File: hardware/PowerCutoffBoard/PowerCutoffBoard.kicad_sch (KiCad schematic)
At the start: 5 parts, among them U1 STM32G431CBUx, U2 MIC4427, U3 MCP2562-E-SN

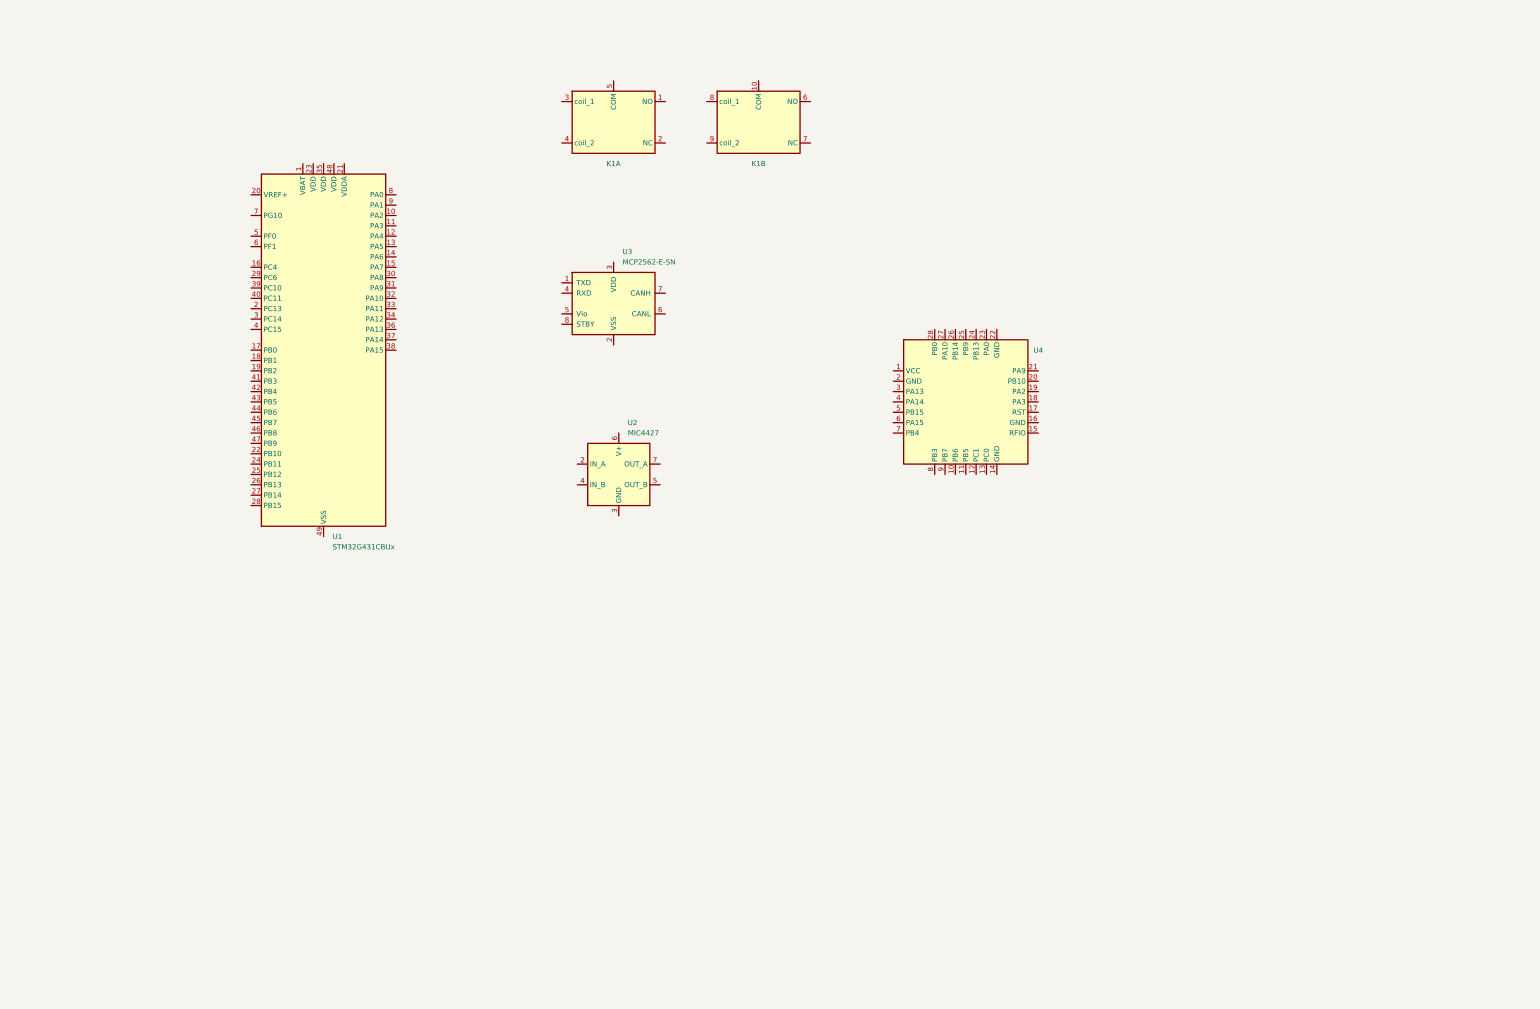
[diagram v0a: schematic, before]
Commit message: update: PowerCutoffBoard's schematic.
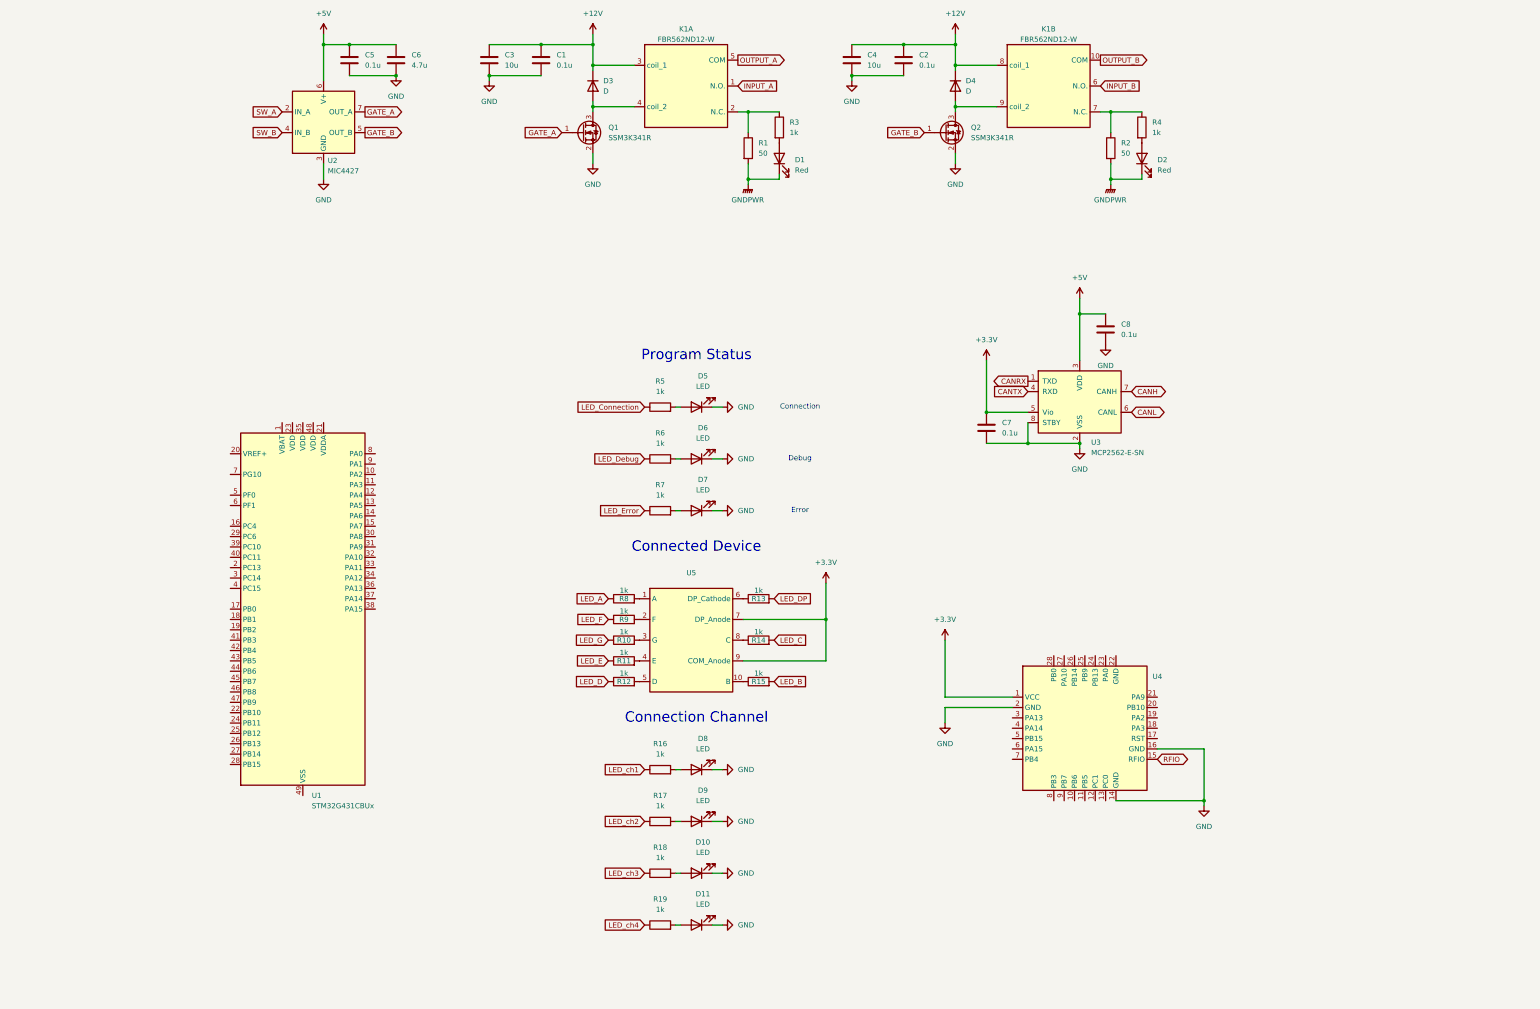
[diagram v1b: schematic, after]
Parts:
- removed K1: ~, GN10_Parts:FBR562, symbol GN10_Parts:Relay_SPDTx2
- added C1, C2, C5, C7, C8: 0.1u, symbol Device:C
- added C3, C4: 10u, symbol Device:C
- added C6: 4.7u, symbol Device:C
- added D1, D2: Red, symbol Device:LED
- added D10, D11, D5, D6, D7, D8, D9: LED, symbol Device:LED
- added D3, D4: D, symbol Device:D
- added K1: FBR562ND12-W, GN10_Parts:FBR562, symbol GN10_Parts:FBR562
- added Q1, Q2: SSM3K341R, symbol Device:Q_NMOS_GSD
- added R1, R2: 50, symbol Device:R
- added R10, R11, R12, R13, R14, R15, R16, R17, R18, R19, R3, R4, R5, R6, R7, R8, R9: 1k, symbol Device:R
- added U5: ~, symbol GN10_Parts:OSL10326_IX
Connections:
- net +3.3V: now reaches U4.1 (VCC)
- net +3.3V: now also U3.5 (Vio), C7.1, U5.7 (DP_Anode), U5.9 (COM_Anode)
- net GND: now reaches U4.14 (GND)
- net GND: now also U2.3 (GND), U3.2 (VSS), U3.8 (STBY), U4.16 (GND), U4.2 (GND), C1.2, C2.2, C3.2, C4.2, C5.2, C6.2, C7.2, C8.2, D10.1 (K), D11.1 (K), D5.1 (K), D6.1 (K), D7.1 (K), D8.1 (K), D9.1 (K), Q1.2 (S), Q2.2 (S)
- net RFIO: now reaches U4.15 (RFIO)
- net SW_A: now reaches U2.2 (IN_A)
- net SW_B: now reaches U2.4 (IN_B)
- net GATE_B: now reaches U2.5 (OUT_B)
- net GATE_B: now also Q2.1 (G)
- net +5V: now reaches U2.6 (V+)
- net +5V: now also U3.3 (VDD), C5.1, C6.1, C8.1
- net GATE_A: now reaches U2.7 (OUT_A)
- net GATE_A: now also Q1.1 (G)
- net CANRX: now reaches U3.1 (TXD)
- net CANTX: now reaches U3.4 (RXD)
- net CANL: now reaches U3.6 (CANL)
- net CANH: now reaches U3.7 (CANH)
- new net: R15.1, U5.10 (B)
- new net: D4.2 (A), K1.9 (coil_2), Q2.3 (D)
- new net: D7.2 (A), R7.2
- new net: D6.2 (A), R6.2
- new net: K1.7 (N.C.), R2.1, R4.1
- new net: R12.2, U5.5 (D)
- new net: D9.2 (A), R17.2
- new net: R8.2, U5.1 (A)
- new net: R9.2, U5.2 (F)
- new net: R10.2, U5.3 (G)
- new net: R11.2, U5.4 (E)
- new net: R13.1, U5.6 (DP_Cathode)
- new net: R14.1, U5.8 (C)
- new net: D3.2 (A), K1.4 (coil_2), Q1.3 (D)
- new net: D11.2 (A), R19.2
- new net: K1.2 (N.C.), R1.1, R3.1
- new net: D8.2 (A), R16.2
- new net: D1.2 (A), R3.2
- new net: D10.2 (A), R18.2
- new net: D5.2 (A), R5.2
- new net: D2.2 (A), R4.2
- new net +12V: C1.1, C2.1, C3.1, C4.1, D3.1 (K), D4.1 (K), K1.3 (coil_1), K1.8 (coil_1)
- new net GNDPWR: D1.1 (K), D2.1 (K), R1.2, R2.2
- new net INPUT_A: K1.1 (N.O.)
- new net INPUT_B: K1.6 (N.O.)
- new net LED_A: R8.1
- new net LED_B: R15.2
- new net LED_C: R14.2
- new net LED_Connection: R5.1
- new net LED_D: R12.1
- new net LED_DP: R13.2
- new net LED_Debug: R6.1
- new net LED_E: R11.1
- new net LED_Error: R7.1
- new net LED_F: R9.1
- new net LED_G: R10.1
- new net LED_ch1: R16.1
- new net LED_ch2: R17.1
- new net LED_ch3: R18.1
- new net LED_ch4: R19.1
- new net OUTPUT_A: K1.5 (COM)
- new net OUTPUT_B: K1.10 (COM)
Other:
- note added: "Connected Device"
- note added: "Connection"
- note added: "Connection Channel"
- note added: "Debug"
- note added: "Error"
- note added: "Program Status"
- moved on the sheet: U1, U2, U3, U4

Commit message: update: PowerCutoffBoard's schematic.
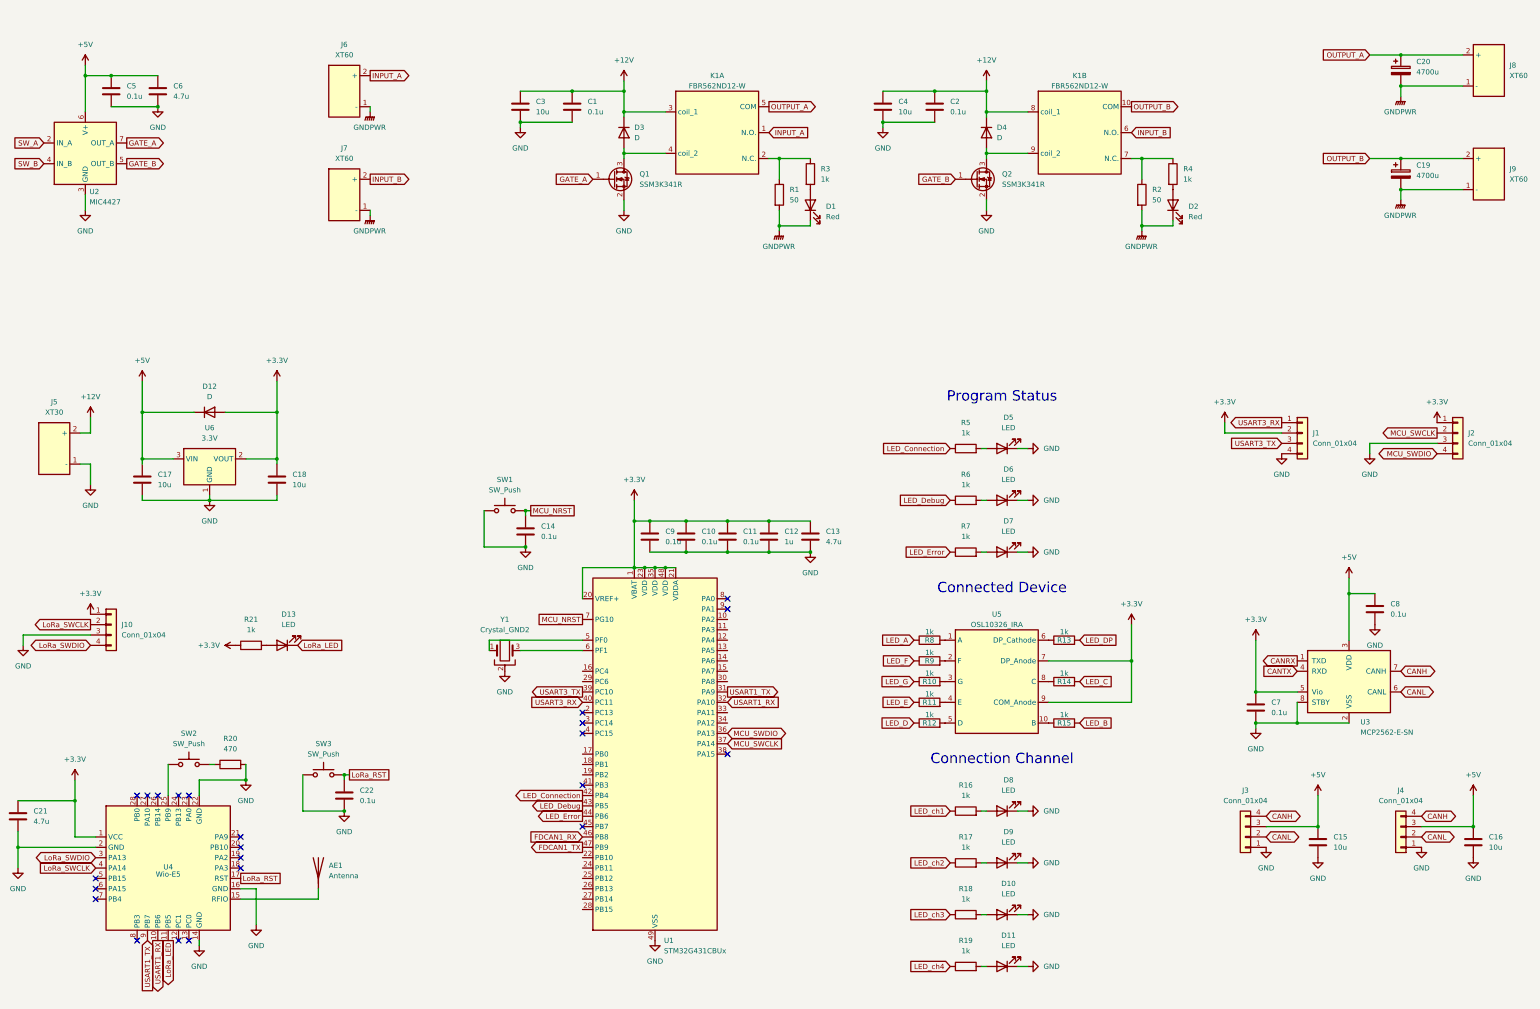
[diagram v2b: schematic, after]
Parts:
- added AE1: Antenna, symbol Device:Antenna
- added C10, C11, C14, C22, C9: 0.1u, symbol Device:C
- added C12: 1u, symbol Device:C
- added C13, C21: 4.7u, symbol Device:C
- added C15, C16, C17, C18: 10u, symbol Device:C
- added C19, C20: 4700u, symbol Device:C_Polarized
- added D12: D, symbol Device:D
- added D13: LED, symbol Device:LED
- added J1, J10, J2, J3, J4: Conn_01x04, symbol Connector_Generic:Conn_01x04
- added J5: XT30, symbol GN10_Parts:XT30
- added J6, J7, J8, J9: XT60, symbol GN10_Parts:XT60
- added R20: 470, symbol Device:R
- added R21: 1k, symbol Device:R
- added SW1, SW2, SW3: SW_Push, symbol Switch:SW_Push
- added U6: 3.3V, Package_TO_SOT_SMD:SOT-223-3_TabPin2, symbol GN10_Parts:TPS1117LV33S
- added Y1: Crystal_GND2, symbol Device:Crystal_GND2
- U4: value ~ -> Wio-E5
- U5: value ~ -> OSL10326_IRA; footprint (none) -> GN10_Parts:OSL10326
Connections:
- net +12V: now also J5.2 (+)
- net +3.3V: now also U1.1 (VBAT), U1.20 (VREF+), U1.21 (VDDA), U1.23 (VDD), U1.35 (VDD), U1.48 (VDD), C10.1, C11.1, C12.1, C13.1, C18.1, C21.1, C9.1, D12.2 (A), J1.2 (Pin_2), J10.1 (Pin_1), J2.1 (Pin_1), R21.1, U6.2 (VOUT)
- net +5V: now also C15.1, C16.1, C17.1, D12.1 (K), J3.3 (Pin_3), J4.3 (Pin_3), U6.3 (VIN)
- net CANH: now also J3.4 (Pin_4), J4.4 (Pin_4)
- net CANL: now also J3.2 (Pin_2), J4.2 (Pin_2)
- net GND: now also U1.49 (VSS), U4.22 (GND), C10.2, C11.2, C12.2, C13.2, C14.2, C15.2, C16.2, C17.2, C18.2, C21.2, C22.2, C9.2, J1.4 (Pin_4), J10.3 (Pin_3), J2.3 (Pin_3), J3.1 (Pin_1), J4.1 (Pin_1), J5.1 (-), R20.2, SW1.1, SW3.1, U6.1 (GND), Y1.2
- net GNDPWR: now also C19.2, C20.2, J6.1 (-), J7.1 (-), J8.1 (-), J9.1 (-)
- net INPUT_A: now also J6.2 (+)
- net INPUT_B: now also J7.2 (+)
- net LED_Connection: now also U1.42 (PB4)
- net LED_Debug: now also U1.43 (PB5)
- net LED_Error: now also U1.44 (PB6)
- net OUTPUT_A: now also C20.1, J8.2 (+)
- net OUTPUT_B: now also C19.1, J9.2 (+)
- net USART1_TX: now reaches U1.31 (PA9)
- net USART1_TX: now also U4.9 (PB7)
- net USART1_RX: now reaches U1.32 (PA10)
- net USART1_RX: now also U4.10 (PB6)
- net MCU_SWDIO: now reaches U1.36 (PA13)
- net MCU_SWDIO: now also J2.4 (Pin_4)
- net MCU_SWCLK: now reaches U1.37 (PA14)
- net MCU_SWCLK: now also J2.2 (Pin_2)
- net USART3_TX: now reaches U1.39 (PC10)
- net USART3_TX: now also J1.3 (Pin_3)
- net USART3_RX: now reaches U1.40 (PC11)
- net USART3_RX: now also J1.1 (Pin_1)
- net FDCAN1_RX: now reaches U1.46 (PB8)
- net FDCAN1_TX: now reaches U1.47 (PB9)
- net at U1.5 (PF0): now also Y1.1
- net at U1.6 (PF1): now also Y1.3
- net MCU_NRST: now reaches U1.7 (PG10)
- net MCU_NRST: now also C14.1, SW1.2
- net LoRa_LED: now reaches U4.11 (PB5)
- net LoRa_LED: now also D13.1 (K)
- net LoRa_RST: now reaches U4.17 (RST)
- net LoRa_RST: now also C22.1, SW3.2
- net at U4.25 (PB9): now also SW2.1
- net LoRa_SWDIO: now reaches U4.3 (PA13)
- net LoRa_SWDIO: now also J10.4 (Pin_4)
- net LoRa_SWCLK: now reaches U4.4 (PA14)
- net LoRa_SWCLK: now also J10.2 (Pin_2)
- net RFIO: no longer names the net of U4.15 (RFIO)
- net RFIO: now also AE1.1 (A)
- new net: D13.2 (A), R21.2
- new net: R20.1, SW2.2
- no-connect marks 0 -> 23
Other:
- note removed: "Connection"
- note removed: "Debug"
- note removed: "Error"
- company: (none) -> Gento Aiba (GN10)
- title: (none) -> GN10PowerCutoffBoard
- moved on the sheet: C1, C2, C3, C4, C5, C6, C7, C8, D1, D10, D11, D2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
